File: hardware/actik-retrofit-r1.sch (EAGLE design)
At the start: 41 parts, among them U13 MAX17055, U5 2450AT18D0100-R, U7 MIC5301, U8 NRF52832, Y1 32MHz, Y4 32.768kHz

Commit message: hw: change few values
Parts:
- C32: value .1u -> 1u
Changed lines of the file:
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@@
 <parts>
 <part name="LICENSE1" library="balto" deviceset="CC_BY-SA" device="" value="Fabio Baltieri"/>
-<part name="C32" library="balto" deviceset="C" device="0603" value=".1u"/>
+<part name="C32" library="balto" deviceset="C" device="0603" value="1u"/>
 <part name="GND41" library="supply1" library_urn="urn:adsk.eagle:library:371" deviceset="GND" device=""/>
 <part name="U7" library="SparkFun-PowerIC" deviceset="V_REG_LDO" device="SMD" value="MIC5301"/>

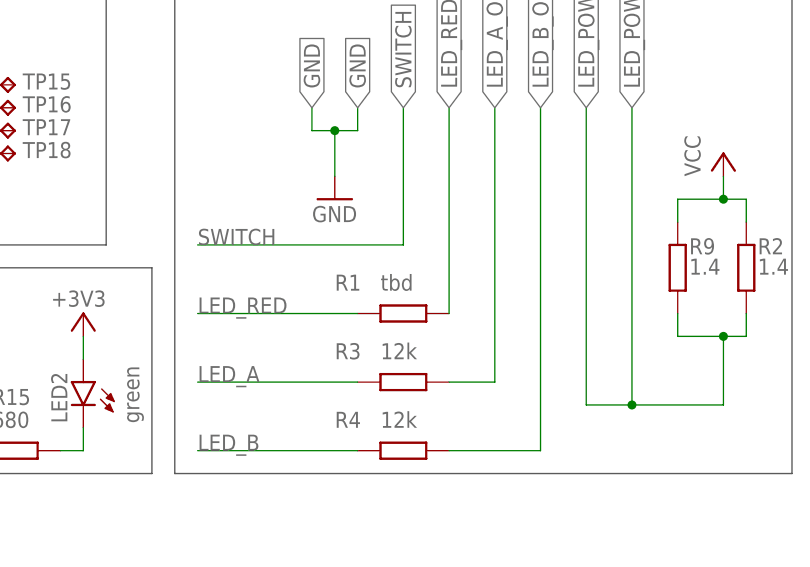
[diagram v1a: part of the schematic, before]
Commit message: hw: actik-r1 set red led res value
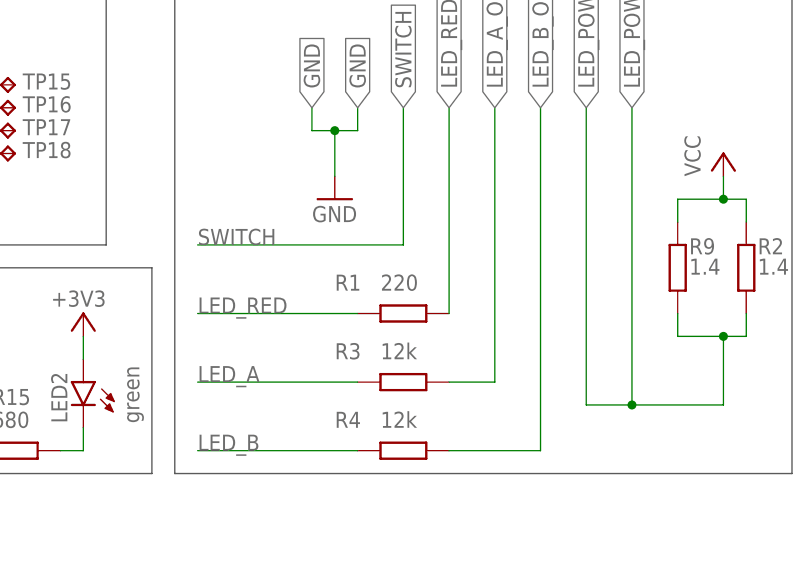
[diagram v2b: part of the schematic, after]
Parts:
- R1: value tbd -> 220
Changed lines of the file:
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@@
 <part name="R9" library="rcl" library_urn="urn:adsk.eagle:library:334" deviceset="R-EU_" device="R3225" package3d_urn="urn:adsk.eagle:package:23549/2" value="1.4"/>
 <part name="R2" library="rcl" library_urn="urn:adsk.eagle:library:334" deviceset="R-EU_" device="R3225" package3d_urn="urn:adsk.eagle:package:23549/2" value="1.4"/>
-<part name="R1" library="balto" deviceset="R" device="0603" value="tbd"/>
+<part name="R1" library="balto" deviceset="R" device="0603" value="220"/>
 <part name="R3" library="balto" deviceset="R" device="0603" value="12k"/>
 <part name="R4" library="balto" deviceset="R" device="0603" value="12k"/>

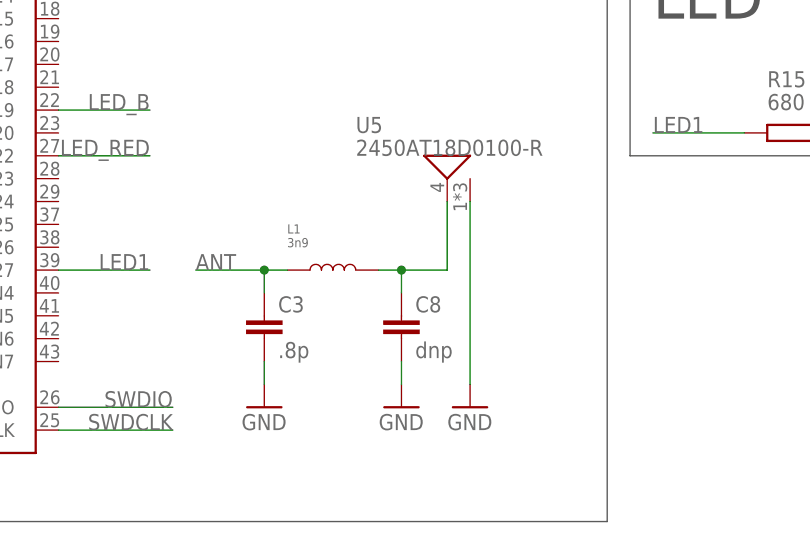
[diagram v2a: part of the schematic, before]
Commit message: hw: actik-r1: annotate schematics for antenna tuning values
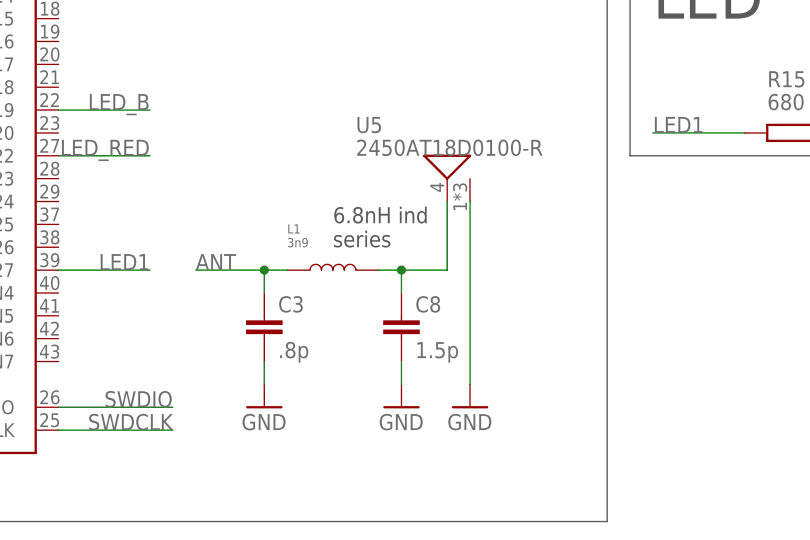
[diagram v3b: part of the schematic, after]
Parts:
- C8: value dnp -> 1.5p
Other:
- note added: "6.8nH ind series"
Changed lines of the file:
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@@
 <?xml version="1.0" encoding="utf-8"?>
 <!DOCTYPE eagle SYSTEM "eagle.dtd">
-<eagle version="9.5.0">
+<eagle version="9.6.2">
 <drawing>
 <settings>
@@
 <part name="C6" library="balto" deviceset="C" device="0603" value="12p"/>
 <part name="C7" library="balto" deviceset="C" device="0603" value="12p"/>
-<part name="C8" library="balto" deviceset="C" device="0603" value="dnp"/>
+<part name="C8" library="balto" deviceset="C" device="0603" value="1.5p"/>
 <part name="GND10" library="supply1" deviceset="GND" device=""/>
 <part name="GND11" library="supply1" deviceset="GND" device=""/>
@@
 <text x="81.28" y="137.16" size="1.778" layer="97">kelvin</text>
 <text x="101.6" y="137.16" size="1.778" layer="97">kelvin</text>
+<text x="106.68" y="35.56" size="1.778" layer="97">6.8nH ind
+series</text>
 </plain>
 <instances>
@@
 </drawing>
 <compatibility>
+<note version="6.3" minversion="6.2.2" severity="warning">
+Since Version 6.2.2 text objects can contain more than one line,
+which will not be processed correctly with this version.
+</note>
 <note version="8.2" severity="warning">
 Since Version 8.2, EAGLE supports online libraries. The ids
